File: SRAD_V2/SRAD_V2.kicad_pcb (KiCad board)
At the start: 4 copper layers, 76.2 x 152.4 mm, 158 parts, among them IC11 op-amp, J1 Conn_01x04_Pin, J5 Conn_01x02_Pin, J6 Conn_01x04_Pin, J7 Conn_01x04_Pin, Q1 MOSFET N-CH, Q2 MOSFET N-CH, Q3 MOSFET N-CH, Q4 MOSFET N-CH, Q5 NPN BJT, U1 Vol Ref., X1 Crystal

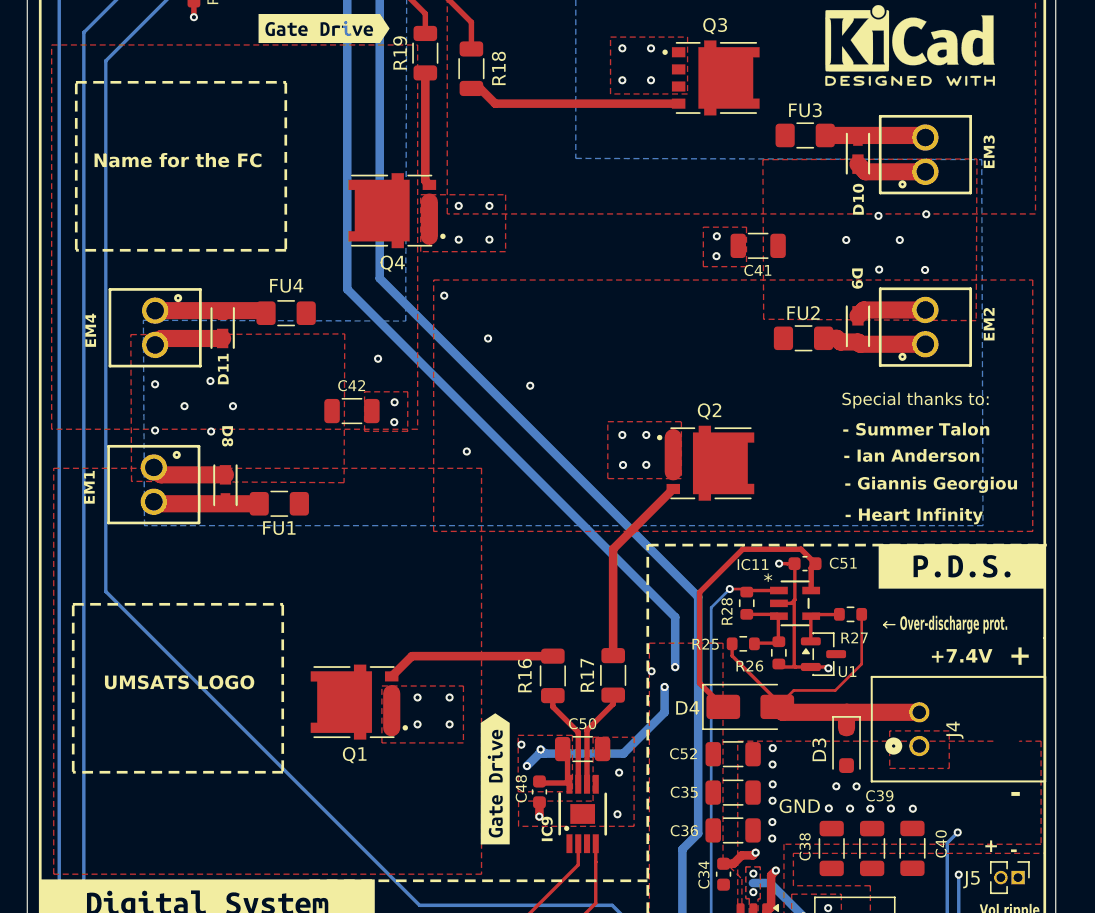
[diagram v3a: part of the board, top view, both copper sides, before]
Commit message: Created Breakout Board Project
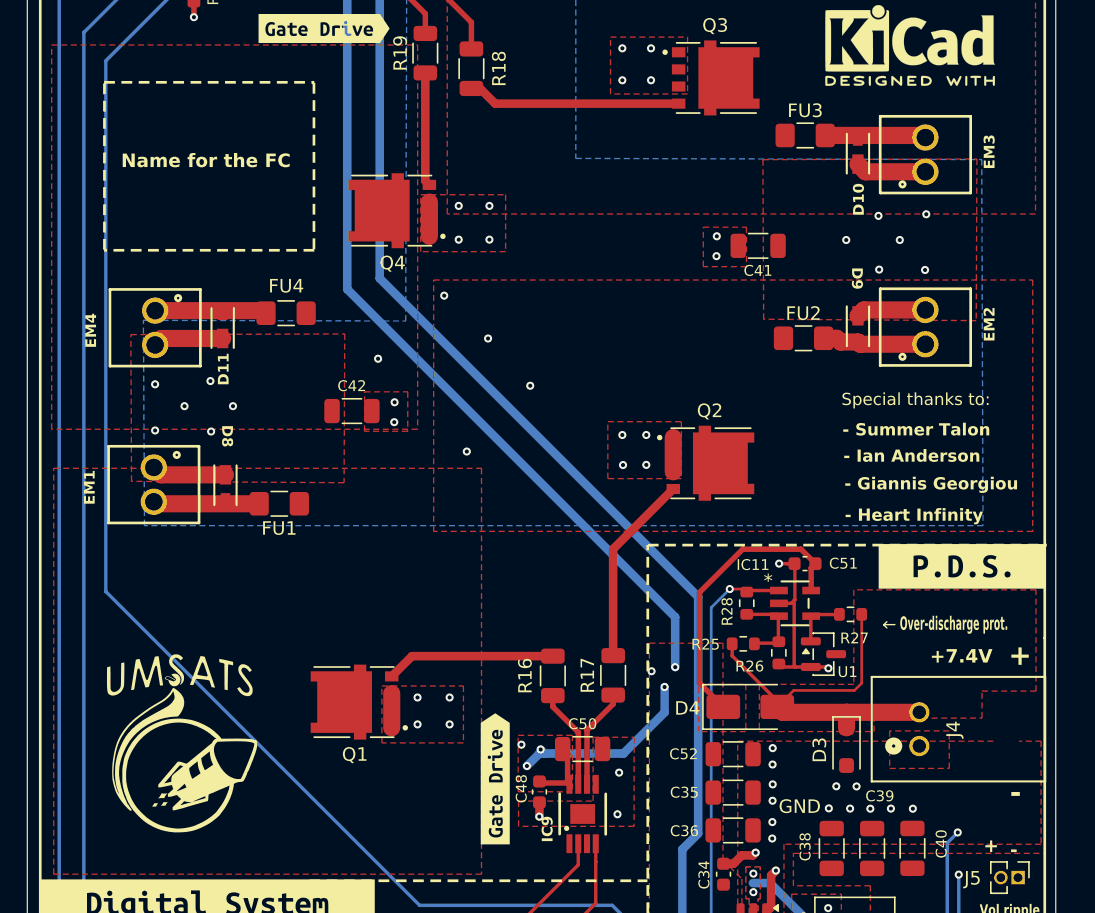
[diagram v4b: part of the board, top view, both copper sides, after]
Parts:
- added G***: LOGO, UMSATS_thick:UMSATS_thick, F.Cu at (67.5, 108.5)
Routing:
- net +7.4V: track 29.2 -> 30.0 mm
- added copper zone on F.Cu, net +7.4V
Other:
- board text removed: "UMSATS LOGO"

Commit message: Updated the 3.3V test point
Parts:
- removed the REF** at (121.7, 57.1)
- added REF**: TestPoint_Pad_2.0x2.0mm, TestPoint:TestPoint_Pad_2.0x2.0mm, F.Cu at (129.7, 114.7)
- J5: value Conn_01x02_Pin -> Conn_01x01_Pin; footprint Connector_PinHeader_1.27mm:PinHeader_1x02_P1.27mm_Vertical -> Connector_PinHeader_1.27mm:PinHeader_1x01_P1.27mm_Vertical
- turned J5 to 0 degrees
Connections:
- J5 pad 1: GND -> /Power Delivery System/+3.3V
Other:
- board text added: "VTP"
- board text removed: "Vol ripple Test point"

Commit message: Ready for fabrication
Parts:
- removed kibuzzard-6A84BD9F: G***, kibuzzard-6A84BD9F
- removed kibuzzard-6A9050AD: G***, kibuzzard-6A9050AD
- removed kibuzzard-6AA6E309: G***, kibuzzard-6AA6E309
- added D12: TVS diode, Diode_SMD:D_SOD-323, F.Cu at (66.8, 158.5)
- added REF**: KiCad-Logo2_5mm_SilkScreen, Symbol:KiCad-Logo2_5mm_SilkScreen, F.Cu at (120.8, 55.7)
- added kibuzzard-6ABFFFA9: G***, kibuzzard-6ABFFFA9, F.Cu at (68.0, 110.2)
- added kibuzzard-6AC049EA: G***, kibuzzard-6AC049EA, F.Cu at (83.5, 159.1)
- added kibuzzard-6AC04A03: G***, kibuzzard-6AC04A03, F.Cu at (108.4, 175.3)
- added kibuzzard-6AC0F9EB: G***, kibuzzard-6AC0F9EB, F.Cu at (59.8, 84.0)
- added kibuzzard-6AC0FA62: G***, kibuzzard-6AC0FA62, F.Cu at (128.6, 71.7)
- moved G*** 25.3 mm to (69.3, 66.7)
- moved G*** 7.46 mm to (67.9, 101.1)
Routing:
- net USB_5V: track 8.09 -> 23.5 mm
- net GND: track 263.8 -> 269.4 mm
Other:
- board text added: "(PCBWay Recommended Stackup)"
- board text added: "3. Impedance Controlled Traces? NO"
- board text added: "FORCS"
- board text added: "MANUFACTURED BY"
- board text added: "PCB Fabrication Notes (Unless specified otherwise):"
- board text added: "Waheguru"
- board text added: "WayWayWay"
- board text removed: "Name for the FC"
- board text removed: "PCB Fabrication Notes:"

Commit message: Minor changes
Minor changes to the srad fab layer(added dimensions) and two traces in the GPS breakout board.
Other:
- board text added: "(3 inches)"
- board text added: "(6 inches)"
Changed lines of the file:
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@@
+		)
+	)
+	(gr_text "(3 inches)"
+		(at 86.375 190.875 0)
+		(layer "F.Fab")
+		(effects
+			(font
+				(size 2 2)
+				(thickness 0.15)
+			)
+			(justify left bottom)
 		)
 	)
@@
 		)
 	)
-	(dimension
-		(type orthogonal)
-		(layer "Dwgs.User")
+	(gr_text "(6 inches)"
+		(at 145.9 110.675 90)
+		(layer "F.Fab")
+		(effects
+			(font
+				(size 2 2)
+				(thickness 0.15)
+			)
+			(justify left bottom)
+		)
+	)
+	(dimension
+		(type orthogonal)
+		(layer "F.Fab")
 		(pts
 			(xy 62 32.5) (xy 62 173.5)
@@
 		)
 		(style
-			(thickness 0.1)
+			(thickness 0.2)
 			(arrow_length 1.27)
-			(text_position_mode 0)
+			(text_position_mode 1)
 			(arrow_direction outward)
 			(extension_height 0.58642)
@@
 		)
 		(gr_text "141mm"
-			(at 52.35 103 90)
-			(layer "Dwgs.User")
-			(effects
-				(font
-					(size 1 1)
-					(thickness 0.15)
-				)
-			)
-		)
-	)
-	(dimension
-		(type orthogonal)
-		(layer "Dwgs.User")
-		(pts
-			(xy 62 173.5) (xy 127 173.5)
-		)
-		(height 7.5)
-		(orientation 0)
-		(format
-			(prefix "")
-			(suffix "mm")
-			(units 2)
-			(units_format 0)
-			(precision 4)
-			(suppress_zeroes yes)
-		)
-		(style
-			(thickness 0.1)
-			(arrow_length 1.27)
-			(text_position_mode 0)
-			(arrow_direction outward)
-			(extension_height 0.58642)
-			(extension_offset 0.5)
-			(keep_text_aligned yes)
-		)
-		(gr_text "65mm"
-			(at 94.5 179.85 0)
-			(layer "Dwgs.User")
-			(effects
-				(font
-					(size 1 1)
-					(thickness 0.15)
-				)
-			)
-		)
-	)
-	(dimension
-		(type orthogonal)
-		(layer "Dwgs.User")
-		(pts
-			(xy 62 32.5) (xy 127 32.5)
-		)
-		(height -8)
-		(orientation 0)
-		(format
-			(prefix "")
-			(suffix "mm")
-			(units 2)
-			(units_format 0)
-			(precision 4)
-			(suppress_zeroes yes)
-		)
-		(style
-			(thickness 0.1)
-			(arrow_length 1.27)
-			(text_position_mode 0)
-			(arrow_direction outward)
-			(extension_height 0.58642)
-			(extension_offset 0.5)
-			(keep_text_aligned yes)
-		)
-		(gr_text "65mm"
-			(at 94.5 23.35 0)
-			(layer "Dwgs.User")
-			(effects
-				(font
-					(size 1 1)
-					(thickness 0.15)
-				)
-			)
-		)
-	)
-	(dimension
-		(type orthogonal)
-		(layer "F.Fab")
-		(pts
-			(xy 56.261004 177.618695) (xy 132.461004 177.618695)
-		)
-		(height 10.009705)
-		(orientation 0)
-		(format
-			(prefix "")
-			(suffix "")
-			(units 2)
-			(units_format 1)
-			(precision 4)
-			(suppress_zeroes yes)
-		)
-		(style
-			(thickness 0.15)
-			(arrow_length 2.54)
-			(text_position_mode 1)
-			(arrow_direction outward)
-			(extension_height 0.58642)
-			(extension_offset 0.5)
-			(keep_text_aligned yes)
-		)
-		(gr_text "76.2 mm"
-			(at 94.361004 187.6284 0)
+			(at 53.5 103 90)
 			(layer "F.Fab")
 			(effects
@@
 		(layer "F.Fab")
 		(pts
-			(xy 132.131004 26.548695) (xy 132.131004 178.948695)
+			(xy 56.261004 176.040295) (xy 132.461004 176.040295)
+		)
+		(height 10.009705)
+		(orientation 0)
+		(format
+			(prefix "")
+			(suffix "")
+			(units 2)
+			(units_format 1)
+			(precision 4)
+			(suppress_zeroes yes)
+		)
+		(style
+			(thickness 0.2)
+			(arrow_length 2.54)
+			(text_position_mode 1)
+			(arrow_direction outward)
+			(extension_height 0.58642)
+			(extension_offset 0.5)
+			(keep_text_aligned yes)
+		)
+		(gr_text "76.2 mm"
+			(at 94.361004 186.05 0)
+			(layer "F.Fab")
+			(effects
+				(font
+					(size 1.5 1.5)
+					(thickness 0.15)
+				)
+			)
+		)
+	)
+	(dimension
+		(type orthogonal)
+		(layer "F.Fab")
+		(pts
+			(xy 62 173.5) (xy 127 173.5)
+		)
+		(height 7.5)
+		(orientation 0)
+		(format
+			(prefix "")
+			(suffix "mm")
+			(units 2)
+			(units_format 0)
+			(precision 4)
+			(suppress_zeroes yes)
+		)
+		(style
+			(thickness 0.2)
+			(arrow_length 1.27)
+			(text_position_mode 1)
+			(arrow_direction outward)
+			(extension_height 0.58642)
+			(extension_offset 0.5)
+			(keep_text_aligned yes)
+		)
+		(gr_text "65mm"
+			(at 94.5 181 0)
+			(layer "F.Fab")
+			(effects
+				(font
+					(size 1.5 1.5)
+					(thickness 0.15)
+				)
+			)
+		)
+	)
+	(dimension
+		(type orthogonal)
+		(layer "F.Fab")
+		(pts
+			(xy 130.236998 26.548695) (xy 130.236998 178.948695)
 		)
 		(height 10.688002)
@@
 		)
 		(style
-			(thickness 0.15)
+			(thickness 0.2)
 			(arrow_length 2.54)
 			(text_position_mode 1)
@@
 		)
 		(gr_text "152.4 mm"
-			(at 142.819006 102.748695 90)
-			(layer "F.Fab")
-			(effects
+			(at 140.925 102.748695 90)
+			(layer "F.Fab")
+			(effects
